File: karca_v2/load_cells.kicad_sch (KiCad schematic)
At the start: 16 parts, among them J4 LoadCell_1_2, J5 LoadCell_3_4, U2 NUP4202, U3 MCP3208, U4 NUP4202, U5 NUP4202, U6 TLV9304xD, U7 TLV9304xD

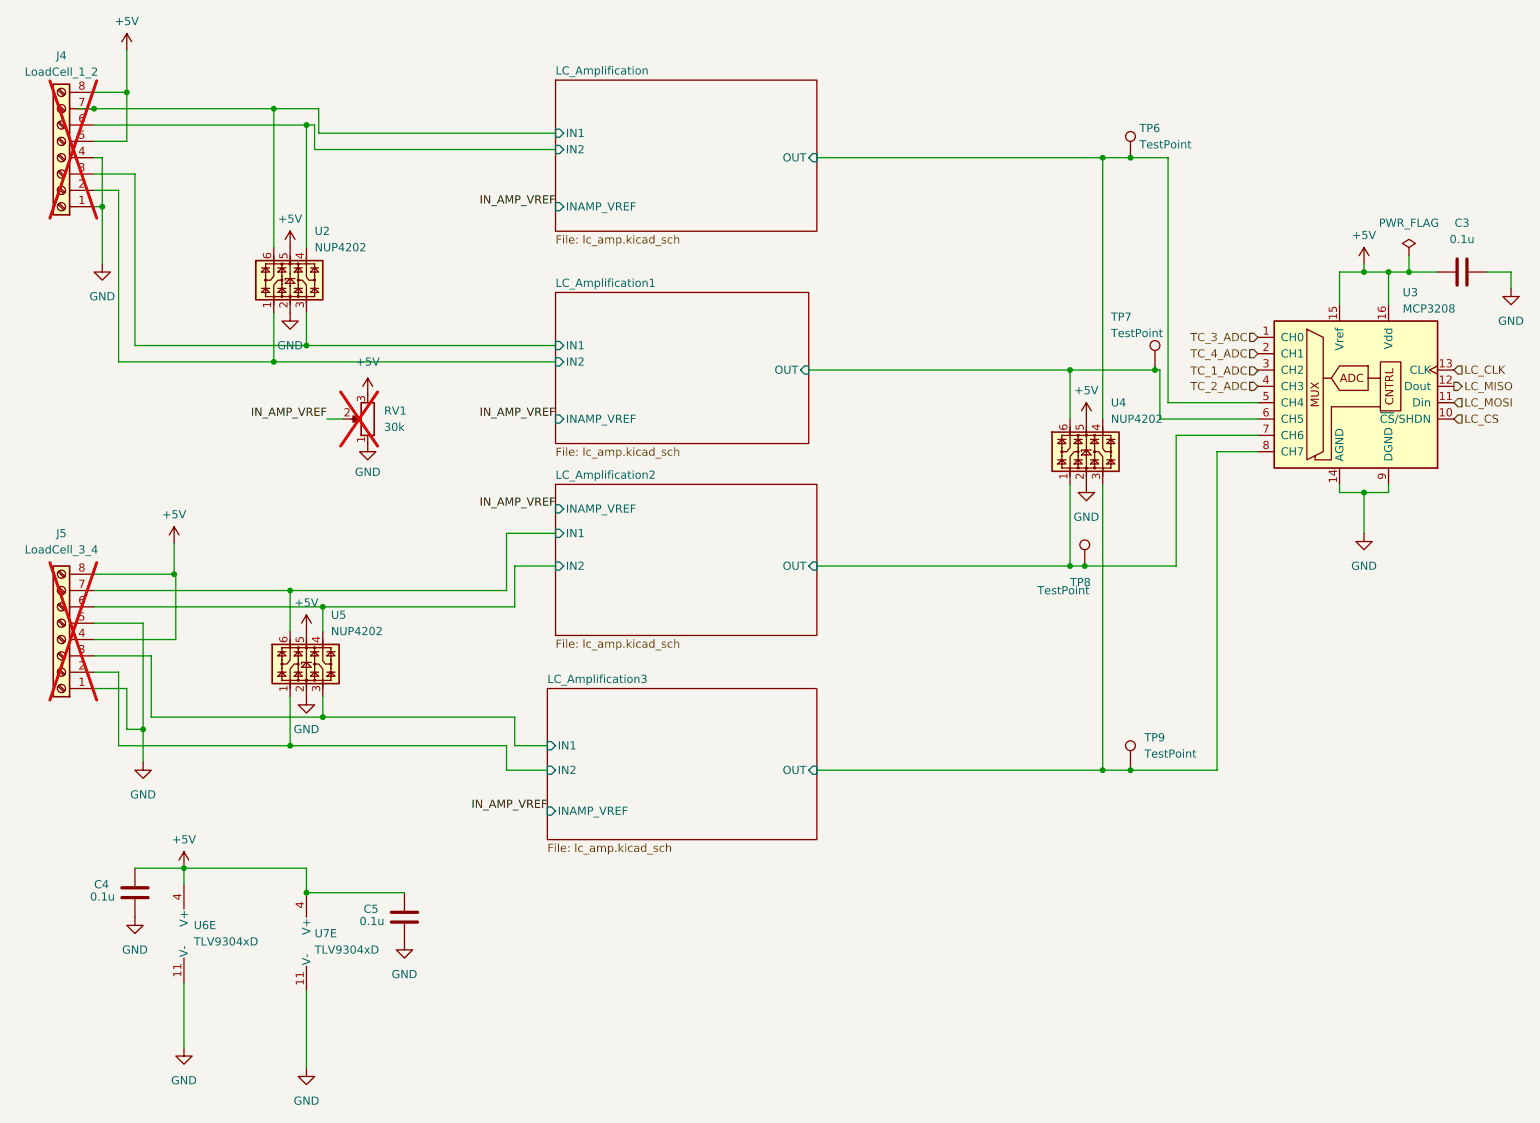
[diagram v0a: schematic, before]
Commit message: added precision shunt reference to ADCs and second SPI bus for driver current and battery voltage monitors
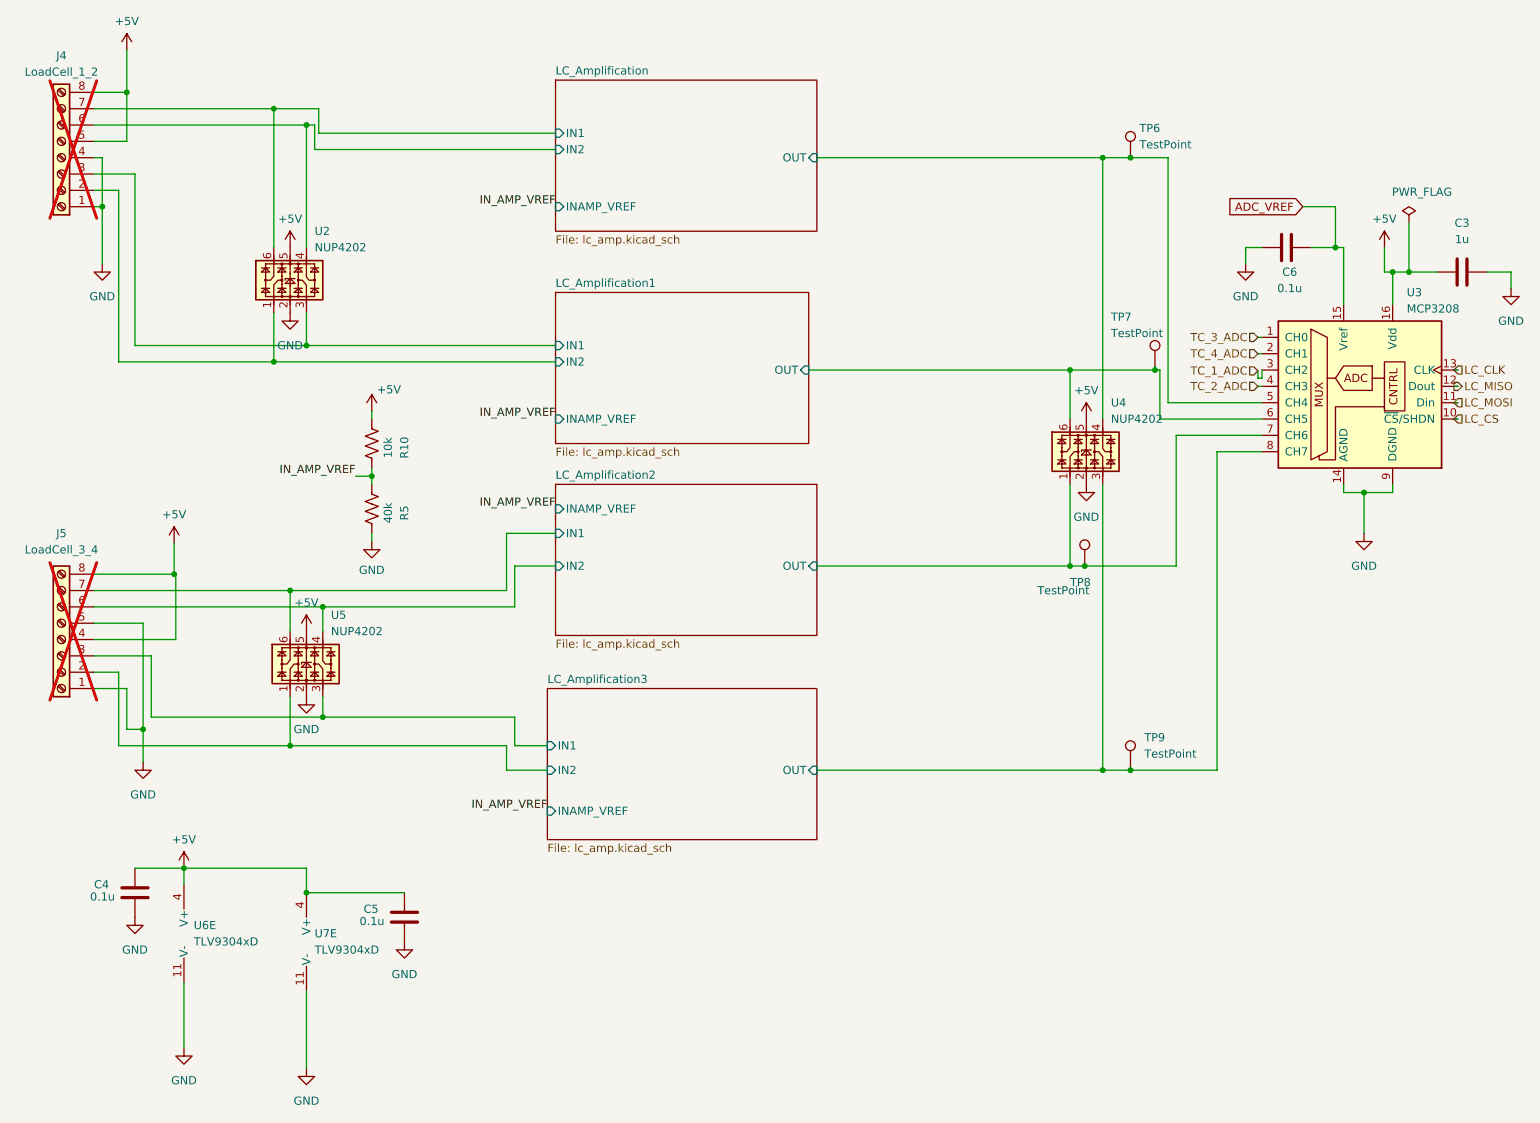
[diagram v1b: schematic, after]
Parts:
- removed RV1: 30k, Potentiometer_THT:Potentiometer_Bourns_3296W_Vertical, symbol Device:R_Potentiometer
- added C6: 0.1u, Capacitor_SMD:C_0805_2012Metric, symbol Device:C
- added R10: 10k, Resistor_SMD:R_1206_3216Metric, symbol Device:R_US
- added R5: 40k, Resistor_SMD:R_1206_3216Metric, symbol Device:R_US
- C3: value 0.1u -> 1u; footprint Capacitor_SMD:C_1206_3216Metric -> Capacitor_SMD:C_0805_2012Metric
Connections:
- net +5V: now also R10.1; no longer U3.15 (Vref)
- net GND: now also C6.1, R5.2
- net IN_AMP_VREF: now also R10.2, R5.1
- new net ADC_VREF: C6.2, U3.15 (Vref)
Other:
- moved on the sheet: U3

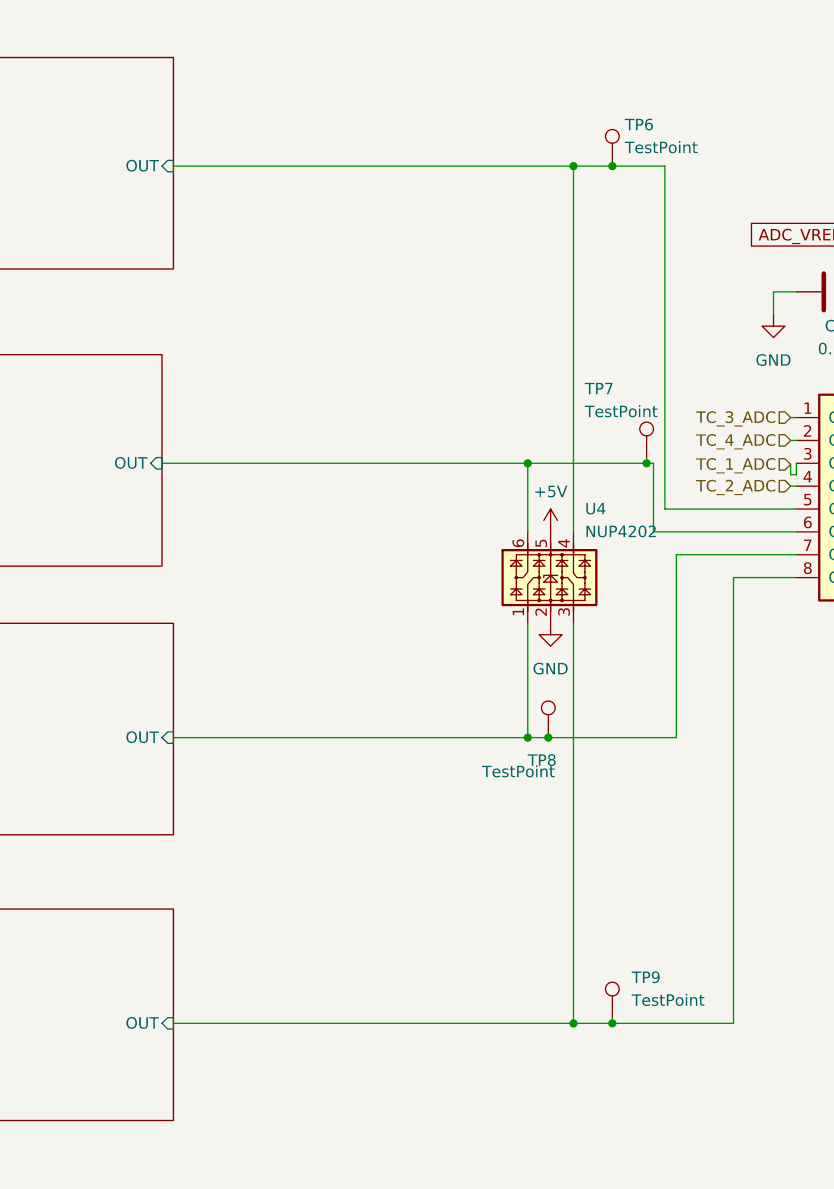
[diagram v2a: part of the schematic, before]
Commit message: fixed all routing. Now need to clean up vias
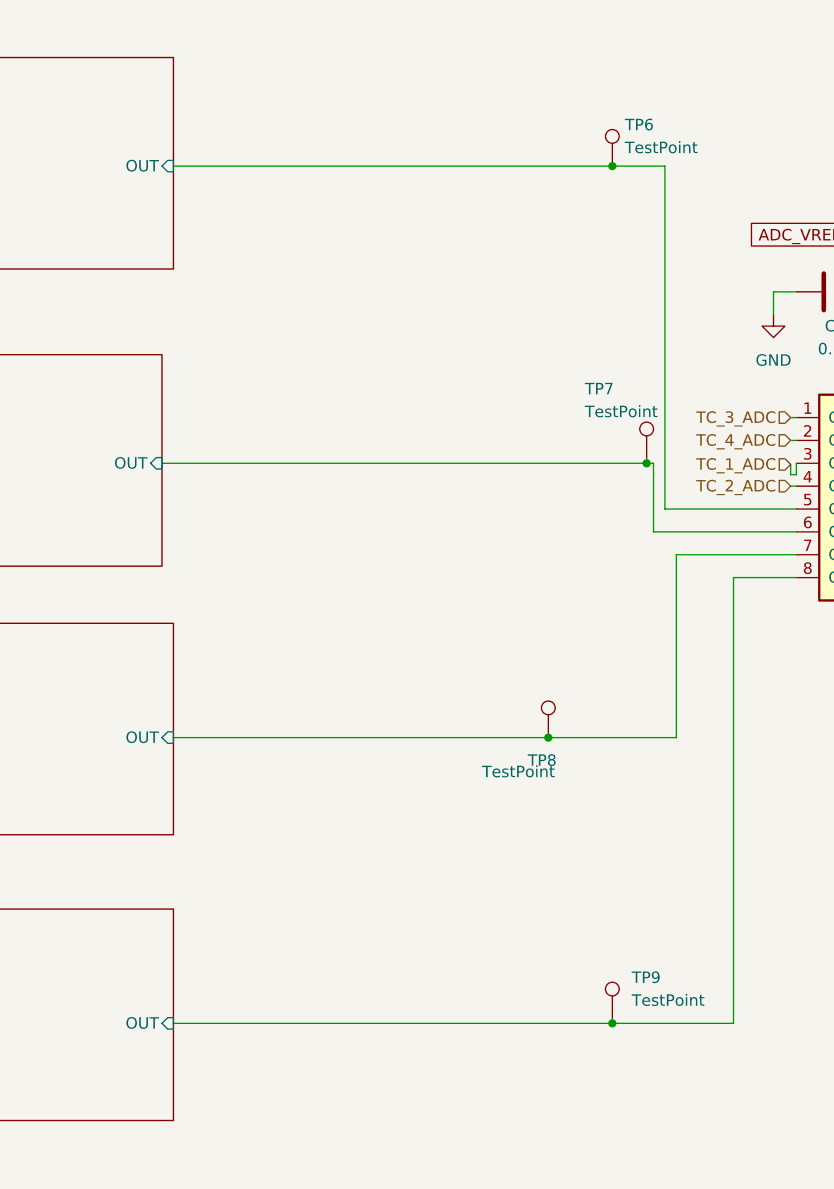
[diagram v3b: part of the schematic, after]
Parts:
- removed U4: NUP4202, Package_TO_SOT_SMD:SOT-363_SC-70-6, symbol Power_Protection:NUP4202
